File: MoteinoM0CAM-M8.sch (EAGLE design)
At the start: 9 parts

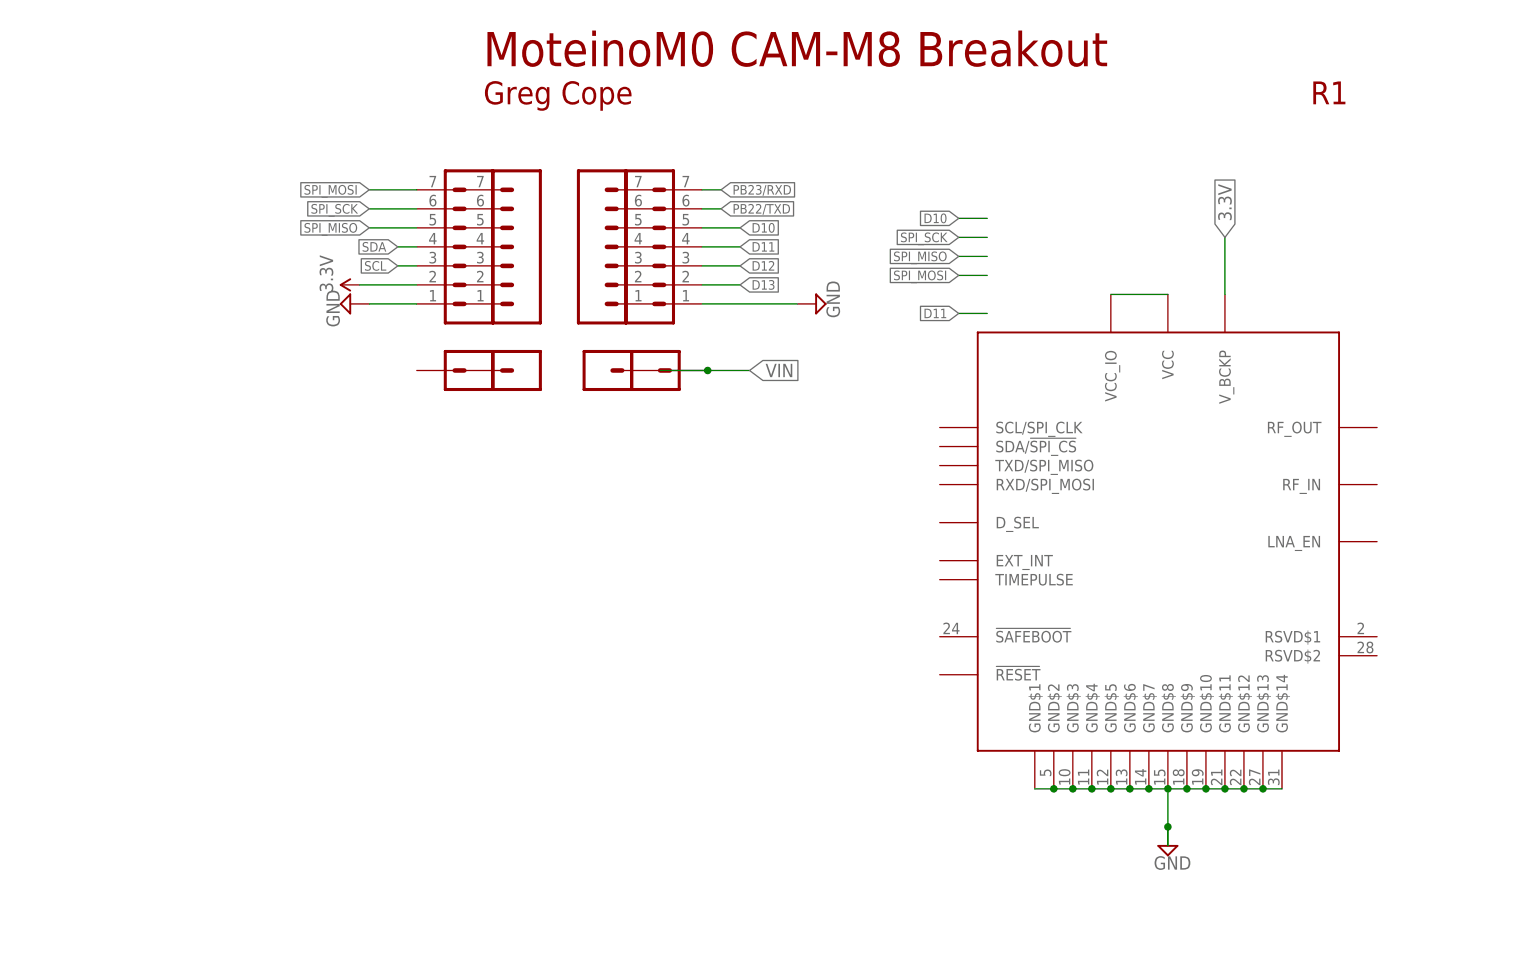
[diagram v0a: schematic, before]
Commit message: Added resistors, led and capacitors
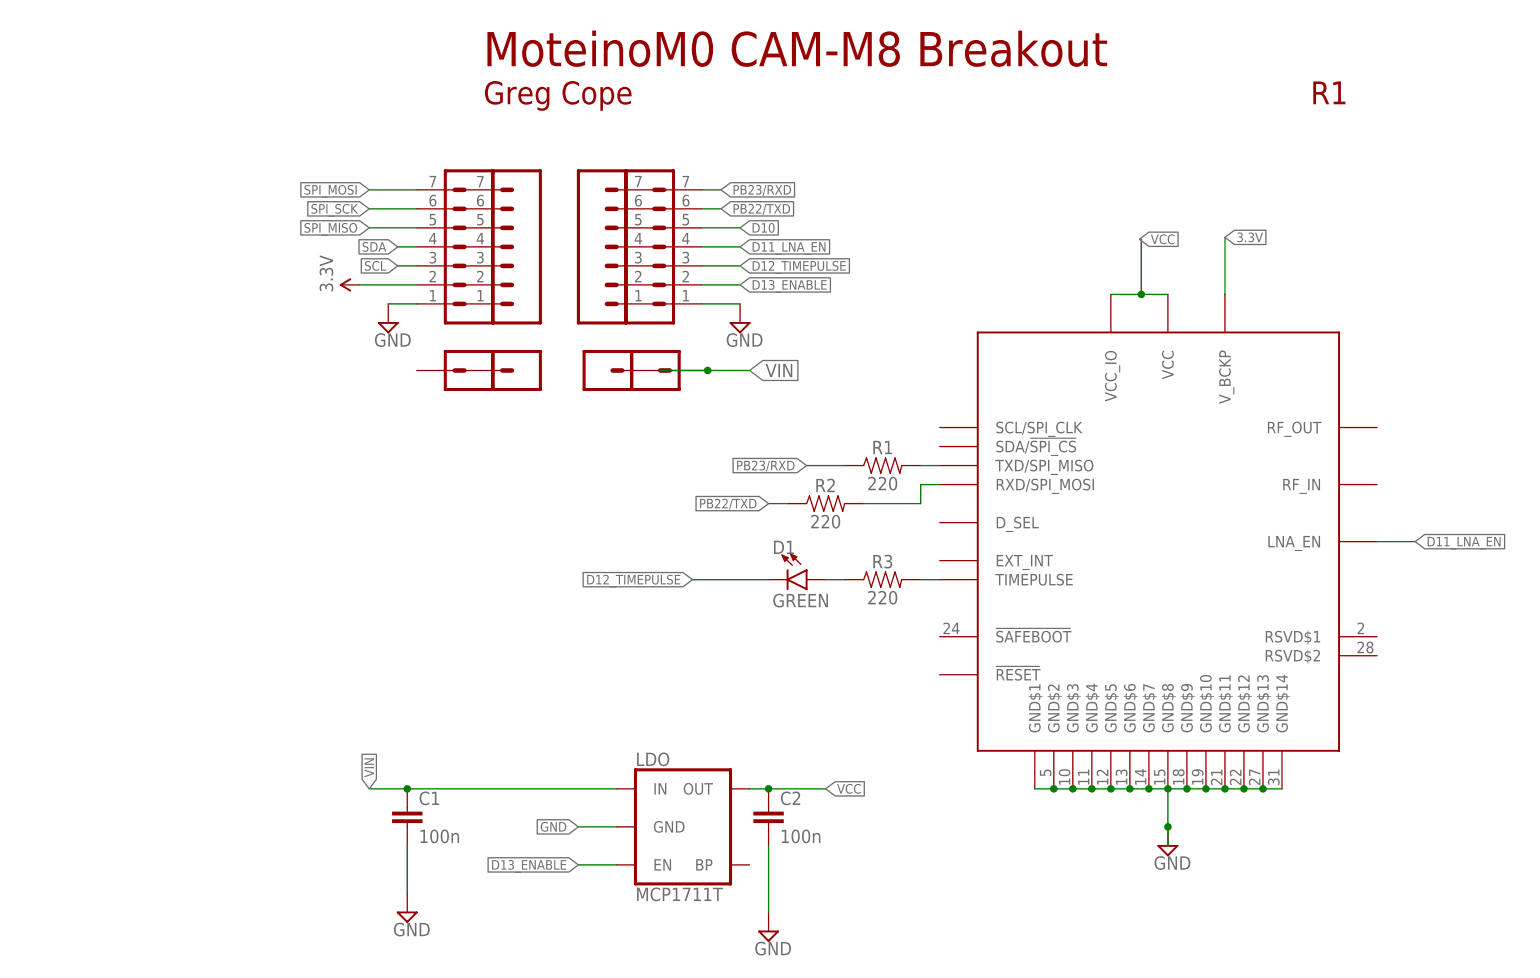
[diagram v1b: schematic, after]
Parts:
- added C1, C2: 100n, SparkFun-Capacitors:0.1UF-0603-25V-5%
- added D1: GREEN, SparkFun-LED:LED-GREEN1206
- added LDO: MCP1711T, SparkFun-IC-Power:V_REG_SPX3819-SOT23-5
- added R1, R2, R3: 220, SparkFun-Resistors:220OHM-0603-1/10W-1%
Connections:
- removed net D11: U$17.4
- removed net D12: U$17.3
- removed net D13: U$17.2
- new net D11_LNA_EN: U$1.LNA_EN, U$17.4
- new net D12_TIMEPULSE: D1.C, U$17.3
- new net D13_ENABLE: LDO.EN, U$17.2
- new net N$1: R3.2, U$1.TIMEPULSE
- new net N$3: R2.2, U$1.RXD/SPI_MOSI
- new net N$4: D1.A, R3.1
- new net VCC: C2.1, LDO.OUT, U$1.VCC, U$1.VCC_IO
- net GND: now also C1.2, C2.2, LDO.GND
- net N$2: now also R1.2, U$1.TXD/SPI_MISO; no longer U$1.VCC, U$1.VCC_IO
- net PB22/TXD: now also R2.1
- net PB23/RXD: now also R1.1
- net VIN: now also C1.1, LDO.IN

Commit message: Doco update III
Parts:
- C1, C2: value 100n -> 100nF
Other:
- note added: "MoteinoM0 CAM-M8Q Breakout"
- note removed: "MoteinoM0 CAM-M8 Breakout"
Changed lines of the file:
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@@
 <part name="J4" library="SparkFun-Connectors" library_urn="urn:adsk.eagle:library:513" deviceset="CONN_01" device="" package3d_urn="urn:adsk.eagle:package:38028/1"/>
 <part name="LDO" library="SparkFun-IC-Power" library_urn="urn:adsk.eagle:library:526" deviceset="V_REG_SPX3819" device="-SOT23-5" package3d_urn="urn:adsk.eagle:package:39060/1" value="MCP1711T"/>
-<part name="C1" library="SparkFun-Capacitors" library_urn="urn:adsk.eagle:library:510" deviceset="0.1UF" device="-0603-25V-5%" package3d_urn="urn:adsk.eagle:package:37414/1" value="100n"/>
-<part name="C2" library="SparkFun-Capacitors" library_urn="urn:adsk.eagle:library:510" deviceset="0.1UF" device="-0603-25V-5%" package3d_urn="urn:adsk.eagle:package:37414/1" value="100n"/>
+<part name="C1" library="SparkFun-Capacitors" library_urn="urn:adsk.eagle:library:510" deviceset="0.1UF" device="-0603-25V-5%" package3d_urn="urn:adsk.eagle:package:37414/1" value="100nF"/>
+<part name="C2" library="SparkFun-Capacitors" library_urn="urn:adsk.eagle:library:510" deviceset="0.1UF" device="-0603-25V-5%" package3d_urn="urn:adsk.eagle:package:37414/1" value="100nF"/>
 <part name="SUPPLY2" library="supply2" library_urn="urn:adsk.eagle:library:372" deviceset="GND" device=""/>
 <part name="SUPPLY3" library="supply2" library_urn="urn:adsk.eagle:library:372" deviceset="GND" device=""/>
@@
 <text x="27.94" y="203.2" size="3.048" layer="94" ratio="12">Greg Cope</text>
 <text x="138.43" y="203.2" size="3.048" layer="94" ratio="12">R1</text>
-<text x="27.94" y="208.28" size="4.572" layer="94" ratio="15">MoteinoM0 CAM-M8 Breakout</text>
+<text x="27.94" y="208.28" size="4.572" layer="94" ratio="15">MoteinoM0 CAM-M8Q Breakout</text>
 </plain>
 <instances>

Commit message: Added images
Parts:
- added C3: 4.7uF, SparkFun-Capacitors:4.7UF0603
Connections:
- net GND: now also C3.2
- net VIN: now also C3.1
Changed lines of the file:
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@@
 <part name="R2" library="SparkFun-Resistors" library_urn="urn:adsk.eagle:library:532" deviceset="220OHM" device="-0603-1/10W-1%" package3d_urn="urn:adsk.eagle:package:39650/1" value="220"/>
 <part name="R3" library="SparkFun-Resistors" library_urn="urn:adsk.eagle:library:532" deviceset="220OHM" device="-0603-1/10W-1%" package3d_urn="urn:adsk.eagle:package:39650/1" value="220"/>
+<part name="C3" library="SparkFun-Capacitors" library_urn="urn:adsk.eagle:library:510" deviceset="4.7UF" device="0603" package3d_urn="urn:adsk.eagle:package:37414/1" value="4.7uF"/>
+<part name="SUPPLY4" library="supply2" library_urn="urn:adsk.eagle:library:372" deviceset="GND" device=""/>
 </parts>
 <sheets>
@@
 <attribute name="NAME" x="81.28" y="141.224" size="1.778" layer="95" font="vector" align="bottom-center"/>
 <attribute name="VALUE" x="81.28" y="138.176" size="1.778" layer="96" font="vector" align="top-center"/>
+</instance>
+<instance part="C3" gate="G$1" x="5.08" y="106.68" smashed="yes">
+<attribute name="NAME" x="6.604" y="109.601" size="1.778" layer="95" font="vector"/>
+<attribute name="VALUE" x="6.604" y="104.521" size="1.778" layer="96" font="vector"/>
+</instance>
+<instance part="SUPPLY4" gate="GND" x="5.08" y="95.25" smashed="yes">
+<attribute name="VALUE" x="3.175" y="92.075" size="1.778" layer="96"/>
 </instance>
 </instances>
@@
 <wire x1="19.05" y1="176.53" x2="15.24" y2="176.53" width="0.1524" layer="91"/>
 </segment>
+<segment>
+<pinref part="C3" gate="G$1" pin="2"/>
+<wire x1="5.08" y1="104.14" x2="5.08" y2="97.79" width="0.1524" layer="91"/>
+<pinref part="SUPPLY4" gate="GND" pin="GND"/>
+</segment>
 </net>
 <net name="SDA" class="0">
@@
 <pinref part="C1" gate="G$1" pin="1"/>
 <wire x1="45.72" y1="111.76" x2="17.78" y2="111.76" width="0.1524" layer="91"/>
-<wire x1="17.78" y1="111.76" x2="12.7" y2="111.76" width="0.1524" layer="91"/>
+<wire x1="17.78" y1="111.76" x2="5.08" y2="111.76" width="0.1524" layer="91"/>
 <junction x="17.78" y="111.76"/>
-<label x="12.7" y="111.76" size="1.27" layer="95" rot="R90" xref="yes"/>
-</segment>
-</net>
+<label x="-2.54" y="111.76" size="1.27" layer="95" rot="R90" xref="yes"/>
+<pinref part="C3" gate="G$1" pin="1"/>
+<wire x1="5.08" y1="111.76" x2="-2.54" y2="111.76" width="0.1524" layer="91"/>
+<junction x="5.08" y="111.76"/>
+</segment>
+</net>

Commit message: Connection tidy, layout tweaks
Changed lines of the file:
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@@
 <wire x1="119.38" y1="111.76" x2="119.38" y2="106.68" width="0.1524" layer="91"/>
 <pinref part="SUPPLY33" gate="GND" pin="GND"/>
-<wire x1="119.38" y1="106.68" x2="119.38" y2="104.14" width="0.1524" layer="91"/>
-<junction x="119.38" y="106.68"/>
 </segment>
 <segment>
